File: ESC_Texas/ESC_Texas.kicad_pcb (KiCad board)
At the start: 4 copper layers, 110 x 57 mm, 68 parts, among them IC1 UCC21331CQDRQ1, IC5 nRF52840-QFAA-F-R7, Q2 IPD100N06S4, Q5 IPD100N06S4, U1 nRF52840, Y1 32MHz, Y2 32.768kHz, Y5 LFSPXO009686, Y6 32MHz

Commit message: ESC project with Aisler settings
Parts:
- removed the C13 at (1.73, 1.00)
- removed the C13 at (125.1, 60.4)
- removed C20, C30, C31: 12pF, Capacitor_SMD:C_0805_2012Metric
- removed C21, C25, C26, C27, C28, C29: 100nF, Capacitor_SMD:C_0805_2012Metric
- removed C32, C_VCC3: 1uF, Capacitor_SMD:C_0805_2012Metric
- removed C33: 47nF, Capacitor_SMD:C_0805_2012Metric
- removed C34: 1.2pF, Capacitor_SMD:C_0805_2012Metric
- removed C35: 100pF, Capacitor_SMD:C_0805_2012Metric
- removed C36: 1pF, Capacitor_SMD:C_0805_2012Metric
- removed C_IN1, C_IN2, C_IN3: 33pF, Capacitor_SMD:C_0805_2012Metric
- removed C_VCC2: 0.8pF, Capacitor_SMD:C_0805_2012Metric
- removed D5, D8: 1N4148WT, Diode_SMD:D_SOD-523
- removed IC5: nRF52840-QFAA-F-R7, nRF52840-QFAA-F-R7:QFN40P600X600X95-49N-D
- removed the L1 at (132.8, 77.0)
- removed the L1 at (122.2, 77.1)
- removed L5: 10uH, Inductor_SMD:L_1008_2520Metric_Pad1.43x2.20mm_HandSolder
- removed L6: 4.7nH, Inductor_SMD:L_1008_2520Metric_Pad1.43x2.20mm_HandSolder
- removed L7: 2.2nH, Inductor_SMD:L_1008_2520Metric_Pad1.43x2.20mm_HandSolder
- removed PS3: MP-K78U15-500R3L, MP-K78U15-500R3L:MPK78U15500R3L
- removed Q5: IPD100N06S4, IPD100N06S4-03:TRANS_BTS3060TFATMA1
- removed U1: nRF52840, Package_DFN_QFN:Nordic_AQFN-73-1EP_7x7mm_P0.5mm
- removed Y1, Y6: 32MHz, Oscillator:Oscillator_SMD_ECS_2520MV-xxx-xx-4Pin_2.5x2.0mm
- removed Y2: 32.768kHz, Oscillator:Oscillator_SMD_ECS_2520MV-xxx-xx-4Pin_2.5x2.0mm
- removed Y5: LFSPXO009686, LFSPXO009686:LFSPXO009686
- added C13: 12pF, Capacitor_SMD:C_0805_2012Metric, F.Cu at (107.2, 51.7)
- added C15: 100pF, Capacitor_SMD:C_0805_2012Metric, F.Cu at (107.2, 57.7)
- added C_1IN1: 33pF, Capacitor_SMD:C_0805_2012Metric, F.Cu at (77.6, 66.3)
- added C_2IN1: 33pF, Capacitor_SMD:C_0805_2012Metric, F.Cu at (77.6, 69.3)
- added C_3IN1: 33pF, Capacitor_SMD:C_0805_2012Metric, F.Cu at (77.6, 72.3)
- added D1: BAS316, Diode_SMD:D_SOD-323, F.Cu at (100.0, 84.1)
- added D3: BAS316, Diode_SMD:D_SOD-323, F.Cu at (100.0, 90.0)
- added IC2: nRF52840-QFAA-F-R7, nRF52840-QFAA-F-R7:QFN40P600X600X95-49N-D, F.Cu at (113.5, 69.3)
- added L1: 15nH, Inductor_SMD:L_1008_2520Metric_Pad1.43x2.20mm_HandSolder, F.Cu at (112.0, 52.0)
- added L2: 10uH, Inductor_SMD:L_1008_2520Metric_Pad1.43x2.20mm_HandSolder, F.Cu at (112.0, 55.8)
- added L3: 4.7nH, Inductor_SMD:L_1008_2520Metric_Pad1.43x2.20mm_HandSolder, F.Cu at (112.0, 59.5)
- added PS1: MP-K78U15-500R3L, MP-K78U15-500R3L:MPK78U15500R3L, F.Cu at (64.5, 54.9)
- added Q1: IPD100N06S4, IPD100N06S4-03:TRANS_BTS3060TFATMA1, F.Cu at (69.3, 68.8)
- added Y3: 32MHz, Oscillator:Oscillator_SMD_ECS_2520MV-xxx-xx-4Pin_2.5x2.0mm, F.Cu at (116.6, 52.3)
- added Y4: Crystal_GND3, Crystal:Crystal_HC52-U-3Pin_Vertical, F.Cu at (99.2, 70.8)
- C10: value 100pF -> 100nF
- C11: value 100pF -> 1pF
- C12: value 100nF -> 12pF
- C14: value 4.7uF -> 1.2pF
- C3, C4: value 12pF -> 100nF
- C6: value 4.7uF -> 100nF
- C7: value 820pF -> 1uF
- C8: value 0.5pf -> 47nF
- C9: value 0.5pF -> 100nF
- D2: value C4D02120E -> BAS316; footprint Package_TO_SOT_SMD:TO-252-2_TabPin1 -> Diode_SMD:D_SOD-323; moved to F.Cu
- L4: value 15nH -> 2.2nH
- moved R_GS_B1 119.3 mm to (82.0, 78.0), turned to 0 degrees
- moved L4 114.7 mm to (112.0, 63.3)
- moved Q2 113.9 mm to (69.3, 76.8)
- moved C_BOOT_A1 91.0 mm to (77.6, 75.3), turned to 0 degrees
- moved R_BOOT_A1 90.5 mm to (82.0, 69.2), turned to 0 degrees
- moved R_GS_A1 90.3 mm to (82.0, 75.1), turned to 0 degrees
- moved RR_ON_B1 81.0 mm to (82.0, 66.2)
- moved R_OFF_B1 73.6 mm to (86.5, 75.1)
- moved R_ON_A1 73.2 mm to (86.5, 78.0)
- moved R_OFF_A1 72.4 mm to (86.5, 72.1)
- moved C_VDD_B1 71.9 mm to (77.6, 87.3), turned to 0 degrees
- moved IC1 70.4 mm to (89.3, 55.9)
- moved D2 68.3 mm to (100.0, 87.0), turned to 0 degrees
- moved C_VCC1 66.8 mm to (77.6, 84.3), turned to 0 degrees
- moved C_EN1 64.6 mm to (77.6, 81.3), turned to 0 degrees
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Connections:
- C10 pad 1: Net-(U1-DEC3) -> GND
- C10 pad 2: Net-(C10-Pad2) -> VDD
- C11 pad 1: Net-(C10-Pad2) -> GND
- C11 pad 2: Net-(U1-DEC4) -> /ANT
- C12 pad 2: Net-(U1-DEC2) -> /XC2
- C14 pad 1: VBUS -> GND
- C14 pad 2: GND -> Net-(C14-Pad2)
- C3 pad 2: Net-(U1-XL2/P0.01) -> VDD
- C5 pad 1: GND -> VDD
- C5 pad 2: Net-(U1-DEC1) -> GND
- C6 pad 1: VDD -> GND
- C6 pad 2: GND -> VDD
- C7 pad 1: GND -> DEC6
- C7 pad 2: Net-(U1-DEC5) -> GND
- C8 pad 1: GND -> DEC6
- C8 pad 2: Net-(C8-Pad2) -> GND
- C9 pad 2: Net-(C8-Pad2) -> VDD
- C_VDD_B1 pad 1: VDD -> +15V
- D2 pad 1: /Driver_subsheet_1/VDDA -> Net-(D2-K)
- D2 pad 2: Net-(D2-A) -> /Driver_subsheet_1/GateA
- IC1 pad 11: VDD -> +15V
- L4 pad 1: Net-(IC5-DEC4) -> Net-(C14-Pad2)
- L4 pad 2: Net-(L4-Pad2) -> unconnected-(L4-Pad2)
- R_BOOT_A1 pad 1: VDD -> +15V
- R_BOOT_A1 pad 2: Net-(D2-A) -> Net-(D1-A)
- R_OFF_A1 pad 2: Net-(D8-K) -> Net-(D2-K)
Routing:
- net /Driver_subsheet_1/VSSA: track 2.58 -> 0.00 mm
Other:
- board outline removed

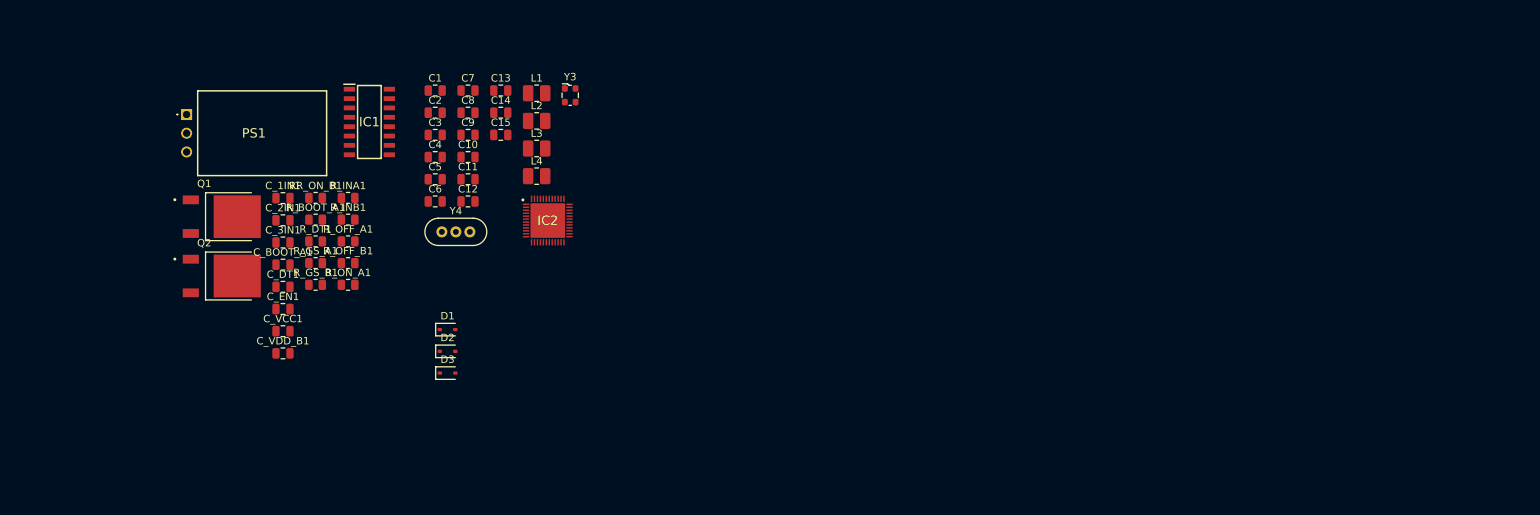
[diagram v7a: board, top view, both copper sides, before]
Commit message: Added pin connections
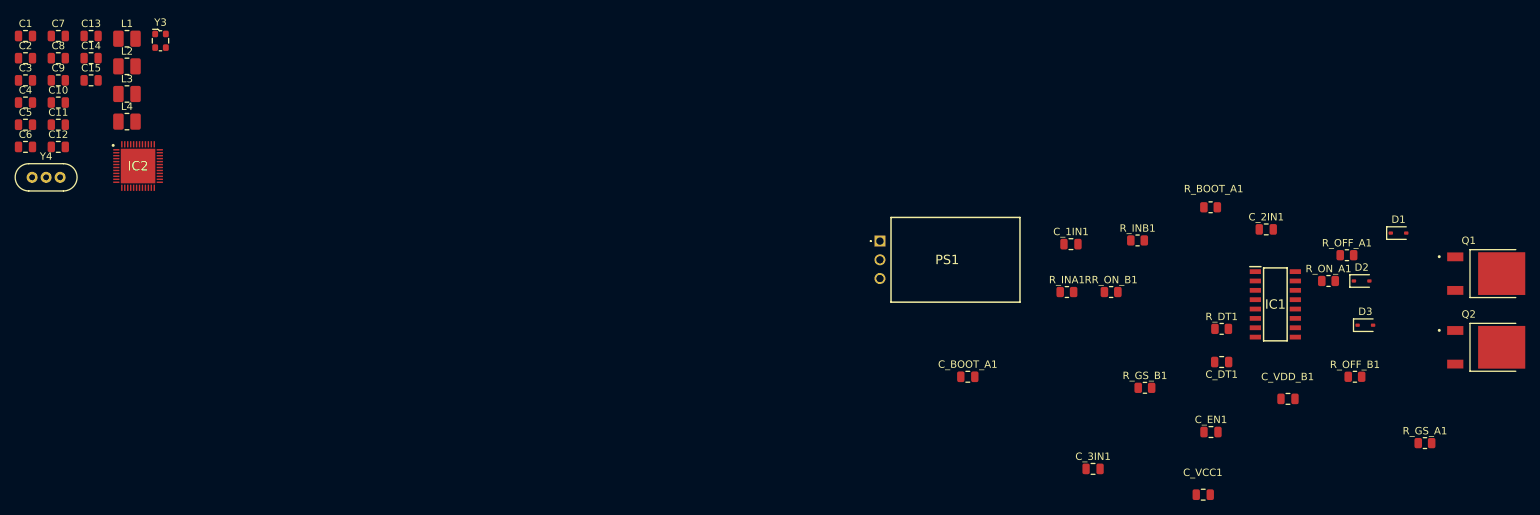
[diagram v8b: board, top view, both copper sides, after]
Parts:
- moved Q2 171.9 mm to (240.9, 86.5)
- moved Q1 171.8 mm to (240.9, 76.5)
- moved R_GS_A1 152.5 mm to (232.6, 99.5)
- moved R_OFF_B1 137.5 mm to (223.1, 90.5)
- moved C_VDD_B1 136.5 mm to (214.0, 93.5)
- moved R_OFF_A1 135.6 mm to (222.0, 74.0)
- moved C_2IN1 133.4 mm to (211.1, 70.5)
- moved R_ON_A1 133.0 mm to (219.5, 77.5)
- moved D1 129.7 mm to (229.0, 71.0)
- moved C_DT1 127.8 mm to (205.0, 88.5), turned to 180 degrees
- moved C_EN1 127.0 mm to (203.6, 98.0)
- moved C_VCC1 126.8 mm to (202.5, 106.5)
- moved IC1 125.4 mm to (212.3, 80.7)
- moved D3 124.7 mm to (224.5, 83.5)
- moved D2 124.4 mm to (224.0, 77.5)
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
